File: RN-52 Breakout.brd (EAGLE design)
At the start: 35.6 x 51.1 mm, 13 parts, among them U1 BLUETOOTH-RN-52

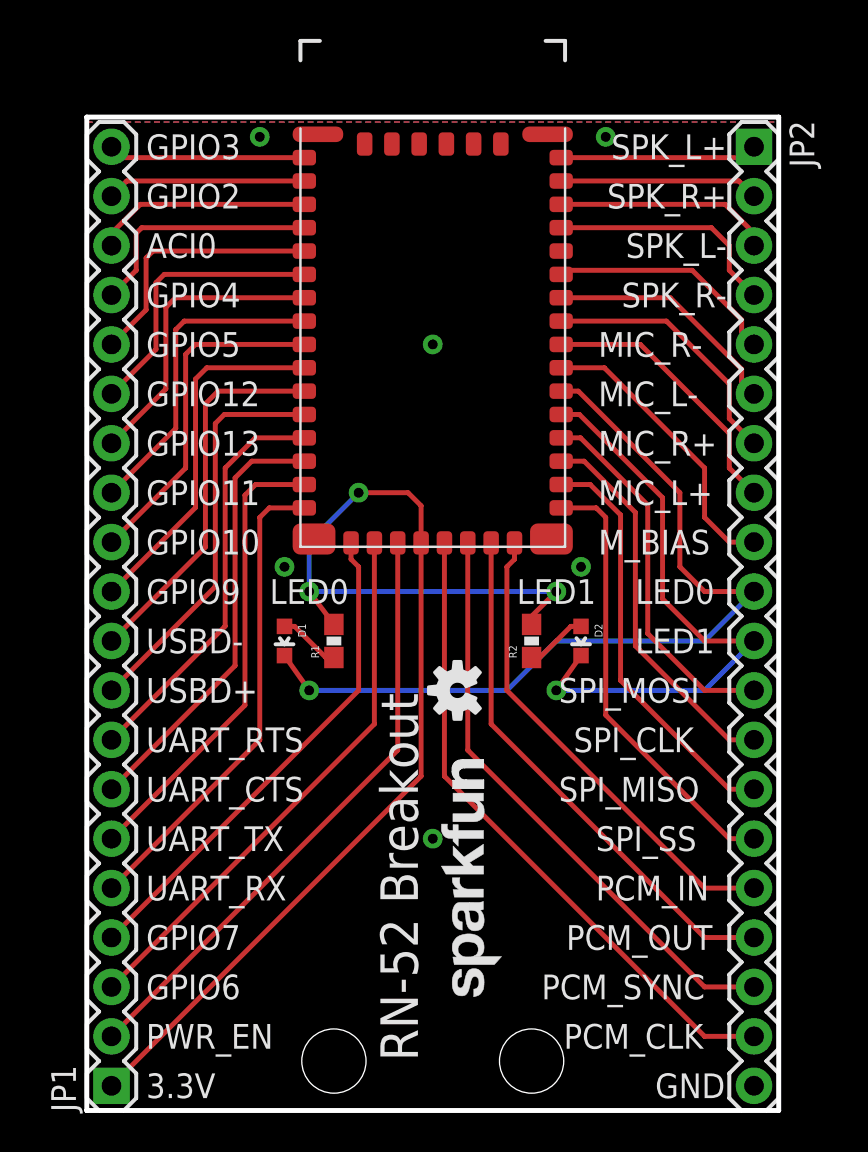
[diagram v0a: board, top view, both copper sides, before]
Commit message: Updated RN-52 to latest footprint
Updated the RN-52 footprint to the latest specs from the newest
datasheet.
Changed some non-45 degree angles to 45 degrees.
Minor silk changes.
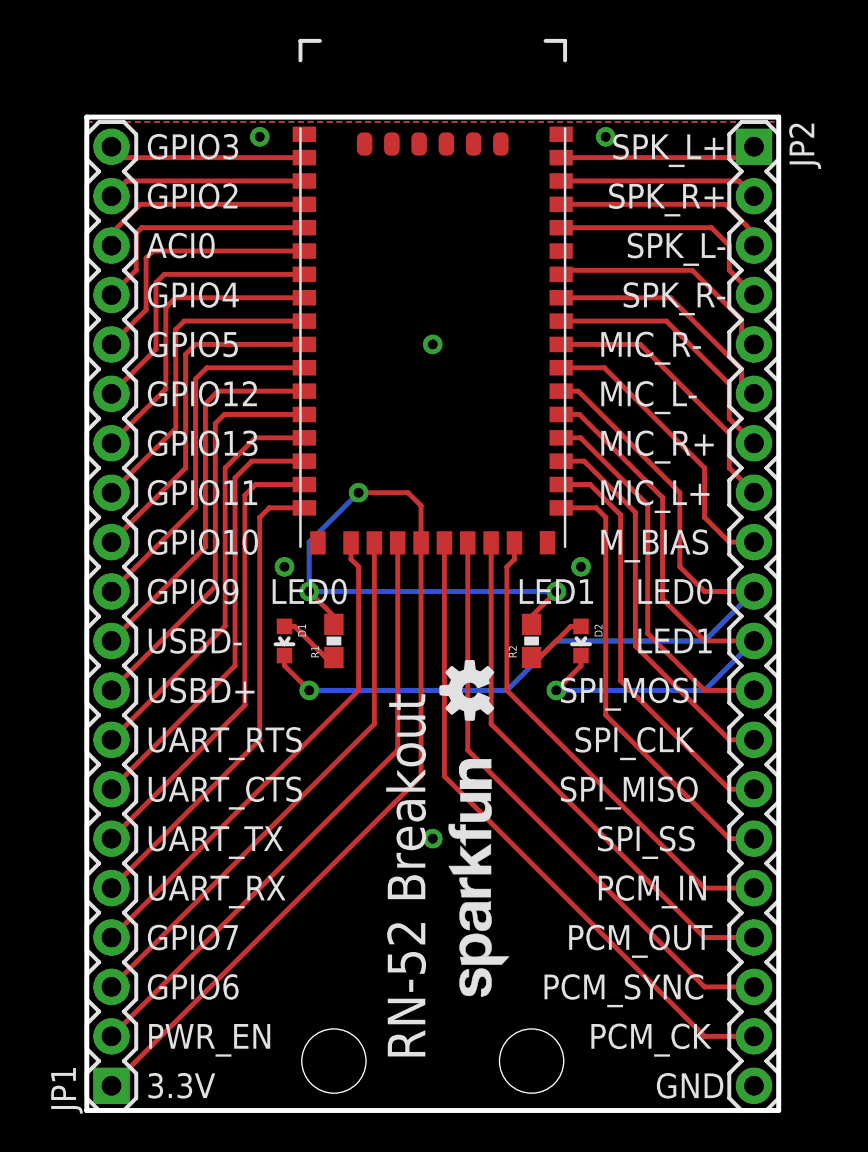
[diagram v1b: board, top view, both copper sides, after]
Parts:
- U1: device SparkFun-RF:RN52 -> SparkFun-RF:RN-52
- moved U1 1.27 mm to (17.8, 40.6)
- moved LOGO1 0.63 mm to (19.7, 21.6)
- moved LOGO4 0.38 mm to (21.7, 5.84)
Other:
- board text added: "PCM_CK"
- board text removed: "PCM_CLK"
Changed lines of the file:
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@@
 <?xml version="1.0" encoding="utf-8"?>
 <!DOCTYPE eagle SYSTEM "eagle.dtd">
-<eagle version="6.2">
+<eagle version="6.4">
 <drawing>
 <settings>
@@
 <layer number="106" name="bPlate" color="7" fill="1" visible="no" active="yes"/>
 <layer number="107" name="Crop" color="7" fill="1" visible="no" active="yes"/>
+<layer number="108" name="tplace-old" color="10" fill="1" visible="yes" active="yes"/>
+<layer number="109" name="ref-old" color="11" fill="1" visible="yes" active="yes"/>
 <layer number="116" name="Patch_BOT" color="9" fill="4" visible="no" active="yes"/>
 <layer number="121" name="_tsilk" color="7" fill="1" visible="no" active="yes"/>
@@
 <text x="24.638" y="8.255" size="1.27" layer="21" font="vector" ratio="15">PCM_OUT</text>
 <text x="23.368" y="5.715" size="1.27" layer="21" font="vector" ratio="15">PCM_SYNC</text>
-<text x="24.511" y="3.175" size="1.27" layer="21" font="vector" ratio="15">PCM_CLK</text>
+<text x="25.781" y="3.175" size="1.27" layer="21" font="vector" ratio="15">PCM_CK</text>
 <text x="29.21" y="0.635" size="1.27" layer="21" font="vector" ratio="15">GND</text>
 <wire x1="0" y1="51.054" x2="35.56" y2="51.054" width="0.254" layer="20"/>
@@
 <wire x1="35.56" y1="0" x2="0" y2="0" width="0.254" layer="20"/>
 <wire x1="0" y1="0" x2="0" y2="51.054" width="0.254" layer="20"/>
-<text x="17.018" y="2.54" size="1.9304" layer="21" font="vector" ratio="15" rot="R90">RN-52 Breakout</text>
+<text x="17.399" y="2.54" size="1.9304" layer="21" font="vector" ratio="15" rot="R90">RN-52 Breakout</text>
 <text x="22.098" y="26.035" size="1.27" layer="21" font="vector" ratio="15">LED1</text>
 <text x="9.398" y="26.035" size="1.27" layer="21" font="vector" ratio="15">LED0</text>
@@
 <text x="32.512" y="8.255" size="1.27" layer="22" font="vector" ratio="15" rot="MR0">PCM_OUT</text>
 <text x="32.512" y="5.715" size="1.27" layer="22" font="vector" ratio="15" rot="MR0">PCM_SYNC</text>
-<text x="32.512" y="3.175" size="1.27" layer="22" font="vector" ratio="15" rot="MR0">PCM_CLK</text>
+<text x="32.512" y="3.175" size="1.27" layer="22" font="vector" ratio="15" rot="MR0">PCM_CK</text>
 <text x="32.512" y="0.635" size="1.27" layer="22" font="vector" ratio="15" rot="MR0">GND</text>
 </plain>
@@
 </class>
 </classes>
-<designrules>
+<designrules name="default *">
 <description language="en">&lt;b&gt;EAGLE Design Rules&lt;/b&gt;
 &lt;p&gt;
@@
 <param name="dpGapFactor" value="2.5"/>
 <param name="checkGrid" value="0"/>
-<param name="checkAngle" value="0"/>
+<param name="checkAngle" value="1"/>
 <param name="checkFont" value="1"/>
 <param name="checkRestrict" value="1"/>
@@
 </autorouter>
 <elements>
-<element name="U1" library="SparkFun-RF" package="RN52" value="BLUETOOTH-RN-52" x="17.78" y="39.37"/>
+<element name="U1" library="SparkFun-RF" package="RN-52" value="BLUETOOTH-RN-52" x="17.78" y="40.64"/>
 <element name="FRAME1" library="SparkFun-Aesthetics" package="CREATIVE_COMMONS" value="FRAME-LETTER" x="15.24" y="-21.59"/>
 <element name="D1" library="SparkFun-LED" package="LED-0603" value="GREEN" x="10.16" y="24.13" rot="R180">
@@
 <attribute name="VALUE" value="RED" x="25.4" y="24.13" size="1.778" layer="27" font="vector" ratio="15" rot="R180" display="off"/>
 </element>
-<element name="LOGO1" library="SparkFun-Aesthetics" package="OSHW-LOGO-S" value="OSHW-LOGOS" x="19.05" y="21.59" rot="R90"/>
+<element name="LOGO1" library="SparkFun-Aesthetics" package="OSHW-LOGO-S" value="OSHW-LOGOS" x="19.685" y="21.59" rot="R90"/>
 <element name="JP1" library="SparkFun-Connectors" package="1X20" value="M20" x="1.27" y="1.27" rot="R90"/>
 <element name="JP2" library="SparkFun-Connectors" package="1X20" value="M20" x="34.29" y="49.53" rot="R270"/>
 <element name="LOGO3" library="SparkFun-Aesthetics" package="SFE-NEW-WEBLOGO" value="LOGO-SFENEW" x="21.717" y="26.035" rot="MR270"/>
-<element name="LOGO4" library="SparkFun-Aesthetics" package="SFE-NEW-WEB" value="LOGO-SFENW2" x="21.336" y="5.842" rot="R90"/>
+<element name="LOGO4" library="SparkFun-Aesthetics" package="SFE-NEW-WEB" value="LOGO-SFENW2" x="21.717" y="5.842" rot="R90"/>
 <element name="R1" library="SparkFun-Resistors" package="0603-RES" value="330" x="12.7" y="24.13" rot="R90"/>
 <element name="R2" library="SparkFun-Resistors" package="0603-RES" value="330" x="22.86" y="24.13" rot="R90"/>
@@
 <wire x1="13.97" y1="31.75" x2="11.43" y2="29.21" width="0.254" layer="16"/>
 <wire x1="11.43" y1="29.21" x2="11.43" y2="26.67" width="0.254" layer="16"/>
-<wire x1="12.7" y1="24.98" x2="11.43" y2="26.67" width="0.254" layer="1"/>
+<wire x1="12.7" y1="24.98" x2="12.7" y2="25.4" width="0.254" layer="1"/>
+<wire x1="12.7" y1="25.4" x2="11.43" y2="26.67" width="0.254" layer="1"/>
 </signal>
 <signal name="LED0">
@@
 <wire x1="30.48" y1="27.94" x2="31.75" y2="26.67" width="0.254" layer="1"/>
 <wire x1="31.75" y1="26.67" x2="34.29" y2="26.67" width="0.254" layer="1"/>
-<wire x1="10.16" y1="23.38" x2="11.43" y2="21.59" width="0.254" layer="1"/>
 <via x="11.43" y="21.59" extent="1-16" drill="0.508"/>
 <wire x1="11.43" y1="21.59" x2="21.59" y2="21.59" width="0.254" layer="16"/>
@@
 <wire x1="24.13" y1="24.13" x2="31.75" y2="24.13" width="0.254" layer="16"/>
 <wire x1="31.75" y1="24.13" x2="34.29" y2="26.67" width="0.254" layer="16"/>
+<wire x1="10.16" y1="23.38" x2="10.16" y2="22.86" width="0.254" layer="1"/>
+<wire x1="10.16" y1="22.86" x2="11.43" y2="21.59" width="0.254" layer="1"/>
 </signal>
 <signal name="LED1">
@@
 <wire x1="29.591" y1="26.289" x2="31.75" y2="24.13" width="0.254" layer="1"/>
 <wire x1="31.75" y1="24.13" x2="34.29" y2="24.13" width="0.254" layer="1"/>
-<wire x1="25.4" y1="23.38" x2="24.13" y2="21.59" width="0.254" layer="1"/>
 <via x="24.13" y="21.59" extent="1-16" drill="0.508"/>
 <wire x1="24.13" y1="21.59" x2="31.75" y2="21.59" width="0.254" layer="16"/>
 <wire x1="31.75" y1="21.59" x2="34.29" y2="24.13" width="0.254" layer="16"/>
+<wire x1="25.4" y1="23.38" x2="25.4" y2="22.86" width="0.254" layer="1"/>
+<wire x1="25.4" y1="22.86" x2="24.13" y2="21.59" width="0.254" layer="1"/>
 </signal>
 <signal name="SPI_MOSI">
